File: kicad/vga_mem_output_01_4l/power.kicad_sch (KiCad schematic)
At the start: 23 parts, among them J2 Conn_01x02_Socket, U1 74LS08, U2 74LS08

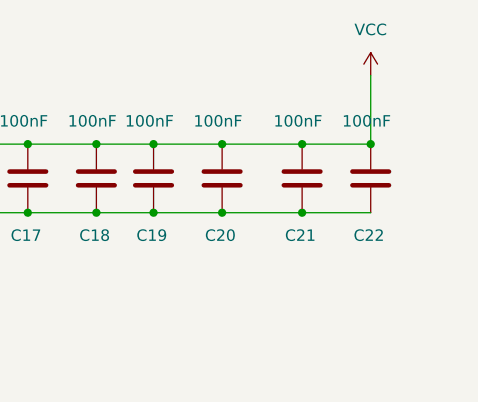
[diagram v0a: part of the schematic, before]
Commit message: finished vga rework
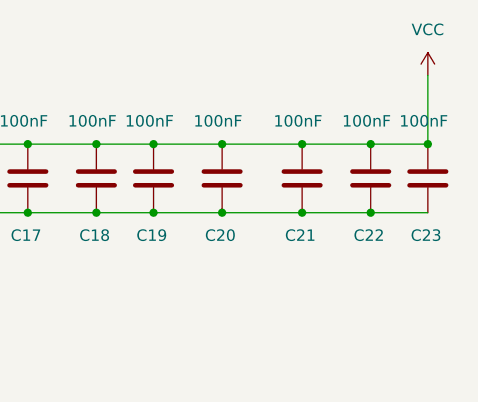
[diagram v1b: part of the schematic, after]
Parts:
- added C23: 100nF, Capacitor_SMD:C_0805_2012Metric_Pad1.18x1.45mm_HandSolder, symbol Device:C
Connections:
- net GND: now also C23.2
- net VCC: now also C23.1
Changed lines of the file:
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@@
+	)
+	(junction
+		(at 316.23 64.77)
+		(diameter 0)
+		(color 0 0 0 0)
 	)
 	(junction
@@
 	)
 	(junction
+		(at 322.58 57.15)
+		(diameter 0)
+		(color 0 0 0 0)
+	)
+	(junction
 		(at 218.44 57.15)
 		(diameter 0)
@@
 	(wire
 		(pts
-			(xy 316.23 49.53) (xy 316.23 57.15)
+			(xy 322.58 49.53) (xy 322.58 57.15)
 		)
 		(stroke
@@
 	(wire
 		(pts
+			(xy 316.23 64.77) (xy 322.58 64.77)
+		)
+		(stroke
+			(width 0)
+			(type default)
+		)
+	)
+	(wire
+		(pts
 			(xy 285.75 64.77) (xy 292.1 64.77)
 		)
@@
 		(pts
 			(xy 247.65 64.77) (xy 255.27 64.77)
+		)
+		(stroke
+			(width 0)
+			(type default)
+		)
+	)
+	(wire
+		(pts
+			(xy 316.23 57.15) (xy 322.58 57.15)
 		)
 		(stroke
@@
 	(symbol
 		(lib_id "Device:C")
+		(at 322.58 60.96 0)
+		(unit 1)
+		(exclude_from_sim no)
+		(in_bom yes)
+		(on_board yes)
+		(dnp no)
+		(property "Reference" "C23"
+			(at 320.675 67.31 0)
+			(effects
+				(font
+					(size 1.27 1.27)
+				)
+				(justify left)
+			)
+		)
+		(property "Value" "100nF"
+			(at 319.405 54.61 0)
+			(effects
+				(font
+					(size 1.27 1.27)
+				)
+				(justify left)
+			)
+		)
+		(property "Footprint" "Capacitor_SMD:C_0805_2012Metric_Pad1.18x1.45mm_HandSolder"
+			(at 323.5452 64.77 0)
+			(effects
+				(font
+					(size 1.27 1.27)
+				)
+				(hide yes)
+			)
+		)
+		(property "Datasheet" "~"
+			(at 322.58 60.96 0)
+			(effects
+				(font
+					(size 1.27 1.27)
+				)
+				(hide yes)
+			)
+		)
+		(property "Description" ""
+			(at 322.58 60.96 0)
+			(effects
+				(font
+					(size 1.27 1.27)
+				)
+			)
+		)
+		(pin "1"
+		)
+		(pin "2"
+		)
+		(instances
+			(project "vga_mem_output_01_4l"
+				(path "/cb13e431-64f0-4016-a936-ee98aca3391f/d37dfd04-5bfb-481b-a0e1-5eb0341e9ca1"
+					(reference "C23")
+					(unit 1)
+				)
+			)
+		)
+	)
+	(symbol
+		(lib_id "Device:C")
 		(at 186.69 60.96 0)
 		(unit 1)
@@
 	(symbol
 		(lib_id "power:VCC")
-		(at 316.23 49.53 0)
+		(at 322.58 49.53 0)
 		(unit 1)
 		(exclude_from_sim no)
@@
 		(dnp no)
 		(property "Reference" "#PWR040"
-			(at 316.23 53.34 0)
+			(at 322.58 53.34 0)
 			(effects
 				(font
@@
 		)
 		(property "Value" "VCC"
-			(at 316.23 44.45 0)
+			(at 322.58 44.45 0)
 			(effects
 				(font
@@
 		)
 		(property "Footprint" ""
-			(at 316.23 49.53 0)
+			(at 322.58 49.53 0)
 			(effects
 				(font
@@
 		)
 		(property "Datasheet" ""
-			(at 316.23 49.53 0)
-			(effects
-				(font
-					(size 1.27 1.27)
-				)
-				(hide yes)
-			)
-		)
-		(property "Description" ""
-			(at 316.23 49.53 0)
-			(effects
-				(font
+			(at 322.58 49.53 0)
+			(effects
+				(font
+					(size 1.27 1.27)
+				)
+				(hide yes)
+			)
+		)
+		(property "Description" ""
+			(at 322.58 49.53 0)
+			(effects
+				(font

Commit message: routing fixes
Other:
- moved on the sheet: C10, C11, C12, C13, C14, C15, C16, C17, C18, C19, C20, C21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

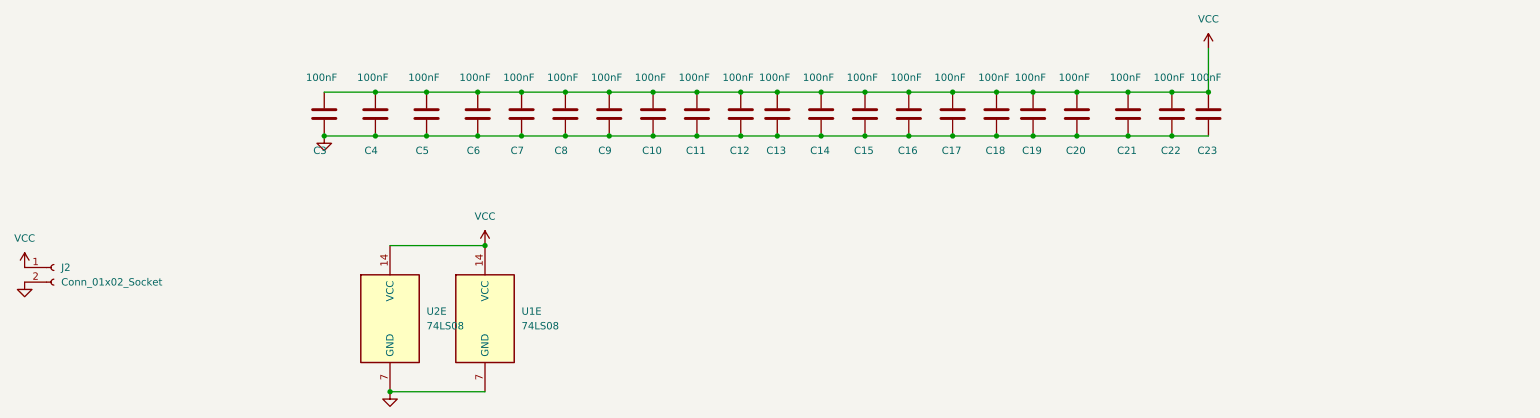
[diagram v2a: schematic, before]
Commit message: switch to VCC pour on signal layers, revised signal / ref assignments
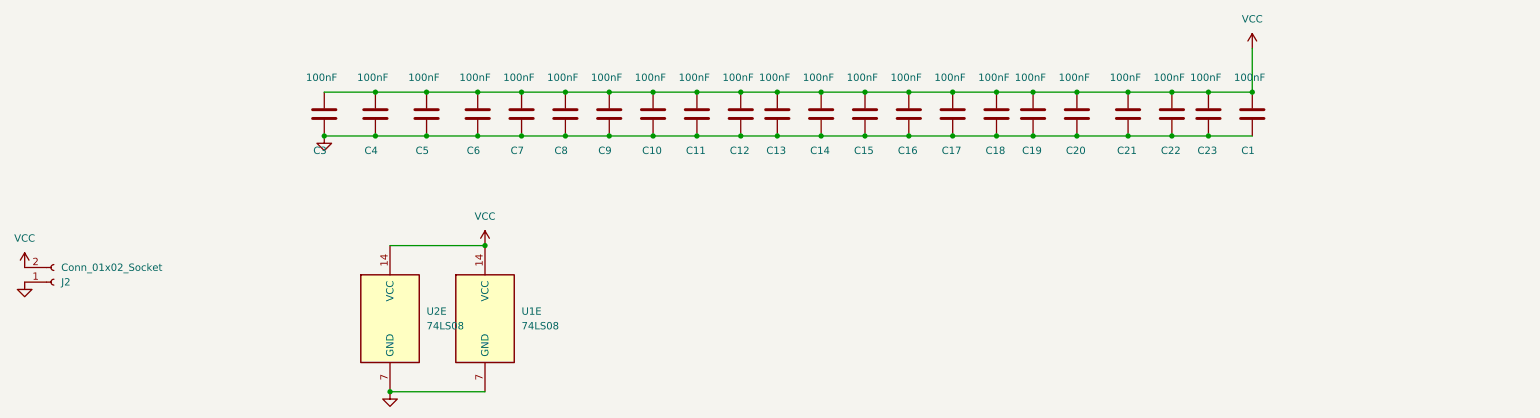
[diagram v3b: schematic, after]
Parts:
- added C1: 100nF, Capacitor_SMD:C_0805_2012Metric_Pad1.18x1.45mm_HandSolder, symbol Device:C
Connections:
- net GND: now also J2.1 (Pin_1), C1.2; no longer J2.2 (Pin_2)
- net VCC: now also J2.2 (Pin_2), C1.1; no longer J2.1 (Pin_1)
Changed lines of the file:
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@@
+	)
+	(junction
+		(at 270.51 36.83)
+		(diameter 0)
+		(color 0 0 0 0)
+	)
+	(junction
+		(at 278.13 29.21)
+		(diameter 0)
+		(color 0 0 0 0)
 	)
 	(junction
@@
 	(wire
 		(pts
+			(xy 270.51 29.21) (xy 278.13 29.21)
+		)
+		(stroke
+			(width 0)
+			(type default)
+		)
+	)
+	(wire
+		(pts
 			(xy 189.23 36.83) (xy 195.58 36.83)
 		)
@@
 	(wire
 		(pts
-			(xy 270.51 21.59) (xy 270.51 29.21)
+			(xy 278.13 21.59) (xy 278.13 29.21)
 		)
 		(stroke
@@
 		(pts
 			(xy 240.03 36.83) (xy 247.65 36.83)
+		)
+		(stroke
+			(width 0)
+			(type default)
+		)
+	)
+	(wire
+		(pts
+			(xy 270.51 36.83) (xy 278.13 36.83)
 		)
 		(stroke
@@
 	(symbol
 		(lib_id "Device:C")
+		(at 278.13 33.02 0)
+		(unit 1)
+		(exclude_from_sim no)
+		(in_bom yes)
+		(on_board yes)
+		(dnp no)
+		(property "Reference" "C1"
+			(at 276.225 39.37 0)
+			(effects
+				(font
+					(size 1.27 1.27)
+				)
+				(justify left)
+			)
+		)
+		(property "Value" "100nF"
+			(at 274.955 26.67 0)
+			(effects
+				(font
+					(size 1.27 1.27)
+				)
+				(justify left)
+			)
+		)
+		(property "Footprint" "Capacitor_SMD:C_0805_2012Metric_Pad1.18x1.45mm_HandSolder"
+			(at 279.0952 36.83 0)
+			(effects
+				(font
+					(size 1.27 1.27)
+				)
+				(hide yes)
+			)
+		)
+		(property "Datasheet" "~"
+			(at 278.13 33.02 0)
+			(effects
+				(font
+					(size 1.27 1.27)
+				)
+				(hide yes)
+			)
+		)
+		(property "Description" ""
+			(at 278.13 33.02 0)
+			(effects
+				(font
+					(size 1.27 1.27)
+				)
+			)
+		)
+		(pin "1"
+		)
+		(pin "2"
+		)
+		(instances
+			(project "vga_mem_output_01_4l"
+				(path "/cb13e431-64f0-4016-a936-ee98aca3391f/d37dfd04-5bfb-481b-a0e1-5eb0341e9ca1"
+					(reference "C1")
+					(unit 1)
+				)
+			)
+		)
+	)
+	(symbol
+		(lib_id "Device:C")
 		(at 256.54 33.02 0)
 		(unit 1)
@@
 	(symbol
 		(lib_id "power:VCC")
-		(at 270.51 21.59 0)
+		(at 278.13 21.59 0)
 		(unit 1)
 		(exclude_from_sim no)
@@
 		(dnp no)
 		(property "Reference" "#PWR040"
-			(at 270.51 25.4 0)
+			(at 278.13 25.4 0)
 			(effects
 				(font
@@
 		)
 		(property "Value" "VCC"
-			(at 270.51 16.51 0)
+			(at 278.13 16.51 0)
 			(effects
 				(font
@@
 		)
 		(property "Footprint" ""
-			(at 270.51 21.59 0)
+			(at 278.13 21.59 0)
 			(effects
 				(font
@@
 		)
 		(property "Datasheet" ""
-			(at 270.51 21.59 0)
-			(effects
-				(font
-					(size 1.27 1.27)
-				)
-				(hide yes)
-			)
-		)
-		(property "Description" ""
-			(at 270.51 21.59 0)
+			(at 278.13 21.59 0)
+			(effects
+				(font
+					(size 1.27 1.27)
+				)
+				(hide yes)
+			)
+		)
+		(property "Description" ""
+			(at 278.13 21.59 0)
 			(effects
 				(font
@@
 	(symbol
 		(lib_id "Connector:Conn_01x02_Socket")
-		(at 69.85 59.69 0)
-		(unit 1)
-		(exclude_from_sim no)
-		(in_bom yes)
-		(on_board yes)
-		(dnp no)
-		(fields_autoplaced yes)
+		(at 69.85 62.23 0)
+		(mirror x)
+		(unit 1)
+		(exclude_from_sim no)
+		(in_bom yes)
+		(on_board yes)
+		(dnp no)
 		(property "Reference" "J2"
-			(at 71.12 59.6899 0)
+			(at 71.12 62.2301 0)
 			(effects
 				(font
@@
 		)
 		(property "Value" "Conn_01x02_Socket"
-			(at 71.12 62.2299 0)
+			(at 71.12 59.6901 0)
 			(effects
 				(font
@@
 		)
 		(property "Footprint" "Connector_PinSocket_2.54mm:PinSocket_1x02_P2.54mm_Vertical"
-			(at 69.85 59.69 0)
+			(at 69.85 62.23 0)
 			(effects
 				(font
@@
 		)
 		(property "Datasheet" "~"
-			(at 69.85 59.69 0)
+			(at 69.85 62.23 0)
 			(effects
 				(font
@@
 		)
 		(property "Description" "Generic connector, single row, 01x02, script generated"
-			(at 69.85 59.69 0)
-			(effects
-				(font
+			(at 69.85 62.23 0)
+			(effects
+				(font
